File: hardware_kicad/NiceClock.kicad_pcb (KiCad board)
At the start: 2 copper layers, 198.2 x 198.2 mm, 294 parts, among them P1 CONN_01X04, U1 WS2811, U10 WS2811, U11 WS2811, U12 WS2811, U13 WS2811, U14 WS2811, U15 WS2811, U16 WS2811, U17 WS2811, U18 WS2811, U19 WS2811, U2 WS2811, U20 WS2811, U21 WS2811, U22 WS2811, U23 WS2811, U24 WS2811, U25 WS2811, U26 WS2811, U27 WS2811, U28 WS2811, U29 WS2811, U3 WS2811, U30 WS2811, U31 WS2811, U32 WS2811, U33 WS2811, U34 WS2811, U35 WS2811, U36 WS2811, U37 WS2811, U38 WS2811, U39 WS2811, U4 WS2811, U40 WS2811, U5 WS2811, U6 WS2811, U7 WS2811, U8 WS2811, U9 WS2811, Y1 8MHz

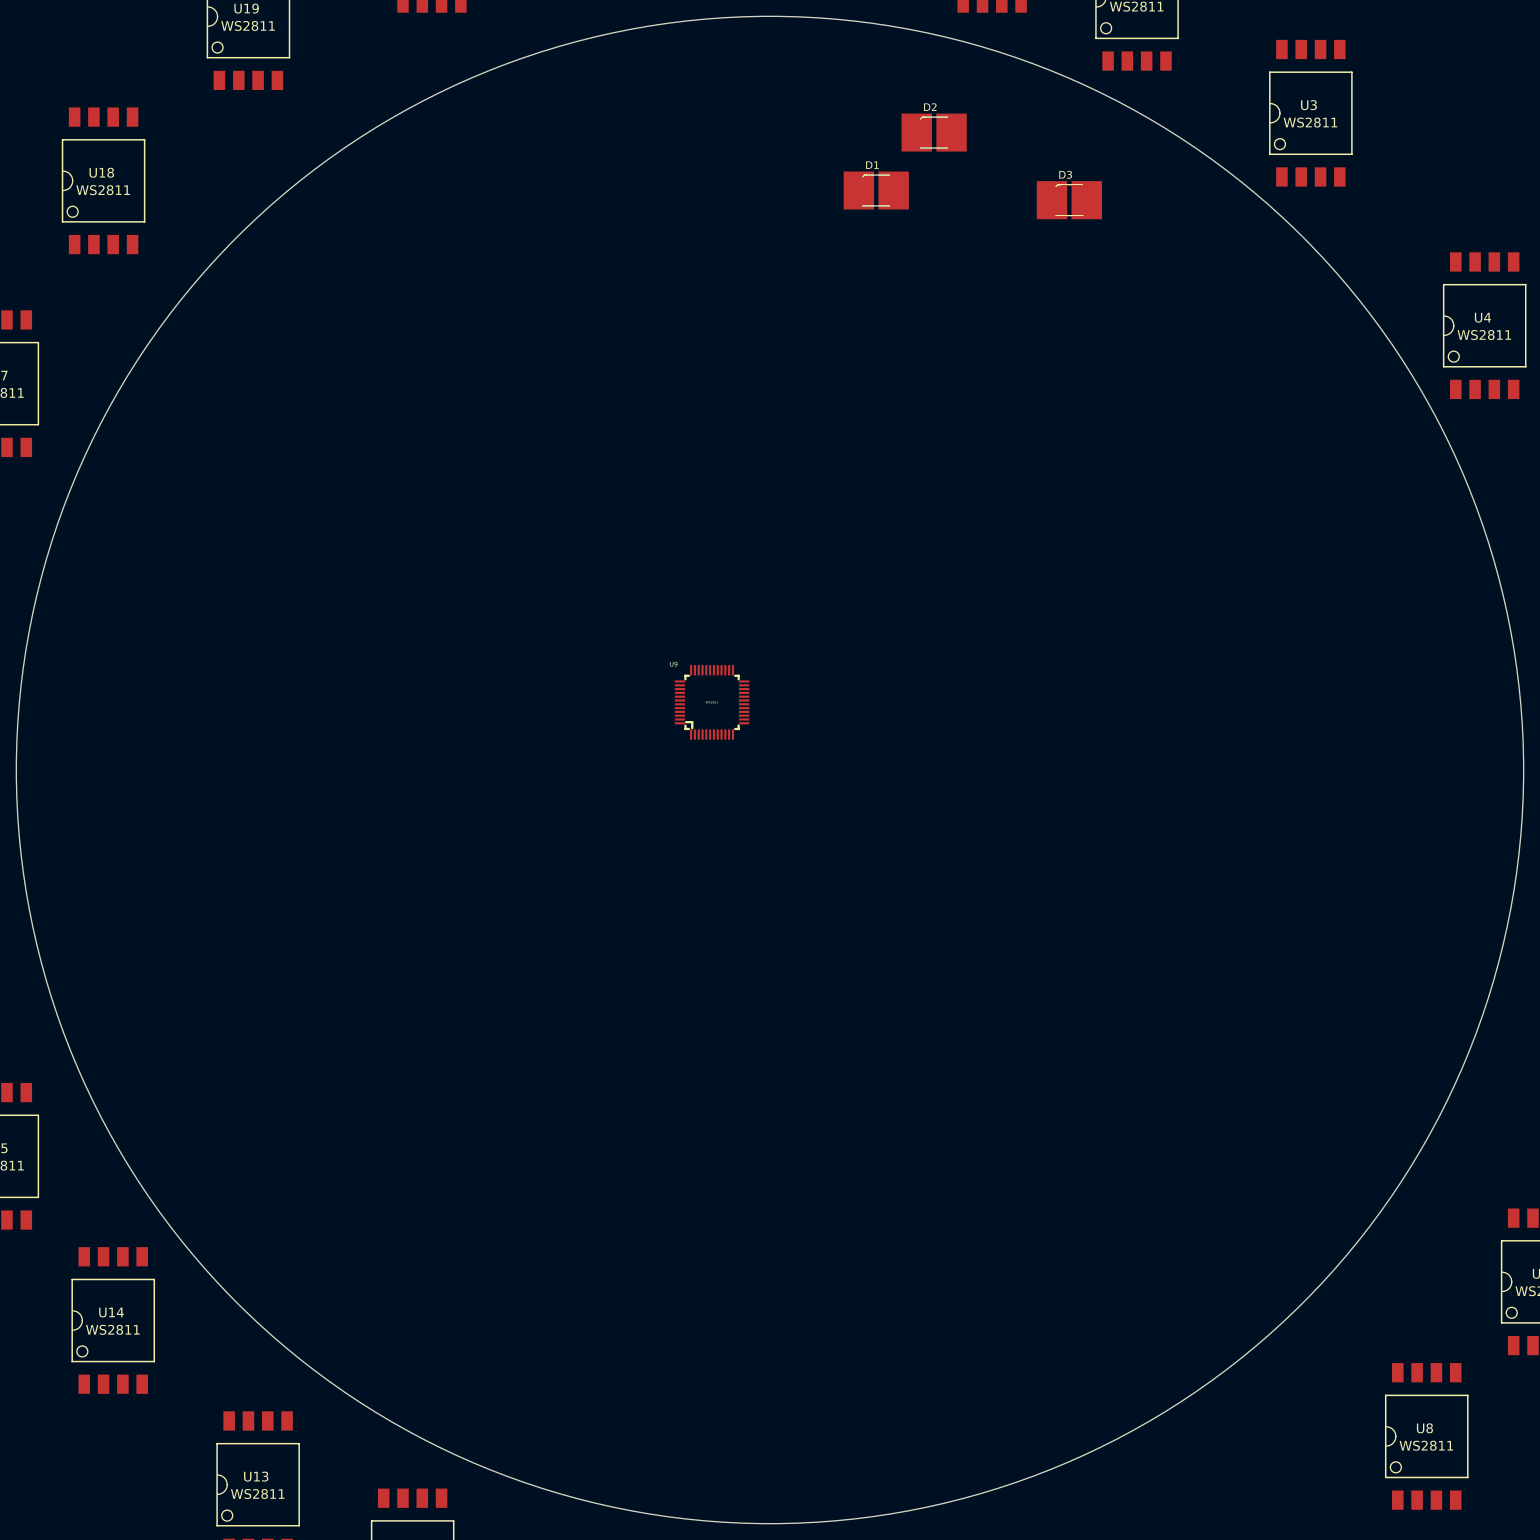
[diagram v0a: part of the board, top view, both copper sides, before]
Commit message: kicad changes + new eagle schematic
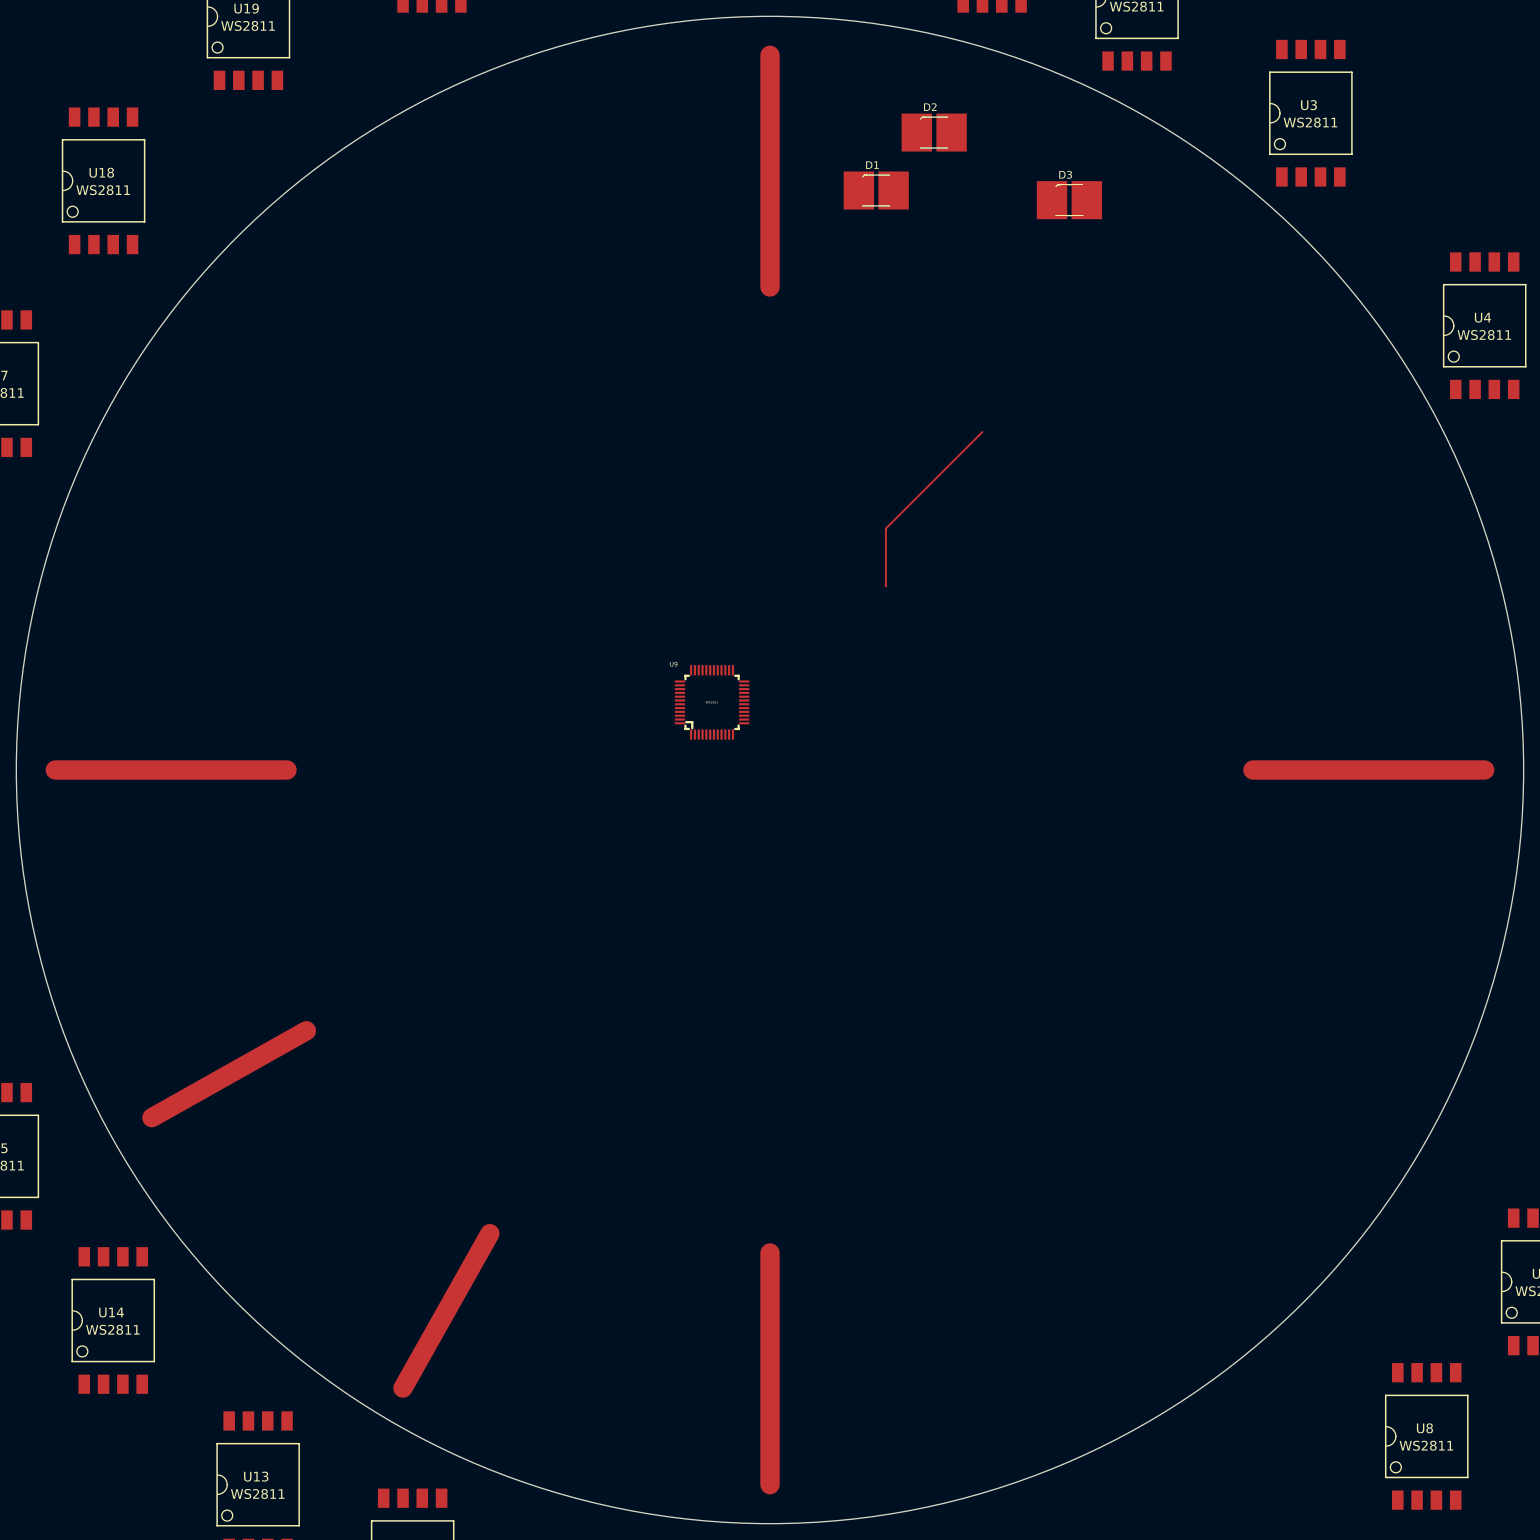
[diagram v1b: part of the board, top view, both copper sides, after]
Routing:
- net (no net): track 0.00 -> 194.1 mm
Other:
- net class Default: trace_width 0.25 -> 2.54
- net class c1 added: clearance 0.2, trace_width 0.5, via_dia 0.6, via_drill 0.4
- net class l1 added: clearance 0.2, trace_width 2.54, via_dia 0.6, via_drill 0.4
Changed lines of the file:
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@@
     (links 762)
     (no_connects 336)
-    (area 106.564302 45.604302 304.915698 243.955698)
+    (area -53.368333 -50.567001 382.370001 294.32819)
     (thickness 1.6)
-    (drawings 6)
-    (tracks 7)
+    (drawings 8)
+    (tracks 15)
     (zones 0)
     (modules 294)
@@
   )
   (setup
-    (last_trace_width 0.25)
+    (last_trace_width 2.54)
     (trace_clearance 0.2)
     (zone_clearance 0.508)
@@
   (net_class Default "This is the default net class."
     (clearance 0.2)
-    (trace_width 0.25)
+    (trace_width 2.54)
     (via_dia 0.6)
     (via_drill 0.4)
@@
     (add_net "Net-(U9-Pad7)")
   )
+  (net_class c1 ""
+    (clearance 0.2)
+    (trace_width 0.5)
+    (via_dia 0.6)
+    (via_drill 0.4)
+    (uvia_dia 0.3)
+    (uvia_drill 0.1)
+  )
+  (net_class l1 ""
+    (clearance 0.2)
+    (trace_width 2.54)
+    (via_dia 0.6)
+    (via_drill 0.4)
+    (uvia_dia 0.3)
+    (uvia_drill 0.1)
+  )
   (module Capacitors_SMD:C_0603_HandSoldering (layer F.Cu)
     (at 242.57 35.56 90)
@@
       (net 6 /OSC_OUT))
   )
+  (gr_circle (center 106.68 143.51) (end 179.07 210.82) (layer Dwgs.User) (width 0.2))
+  (gr_circle (center 205.74 243.84) (end 128.27 181.61) (layer Dwgs.User) (width 0.2))
   (target plus (at 205.74 144.78) (size 5) (width 0.15) (layer Edge.Cuts))
   (gr_line (start 382.27 88.9) (end 382.27 186.69) (angle 90) (layer Dwgs.User) (width 0.2))
@@
   (gr_line (start 205.74 38.1) (end 205.74 251.46) (angle 90) (layer Dwgs.User) (width 0.2))
   (gr_circle (center 205.74 144.78) (end 120.65 93.98) (layer Edge.Cuts) (width 0.15))
+  (segment (start 157.48 226.06) (end 168.91 205.74) (width 2.54) (layer F.Cu) (net 0))
+  (segment (start 124.46 190.5) (end 144.78 179.07) (width 2.54) (layer F.Cu) (net 0))
+  (segment (start 205.74 238.76) (end 205.74 208.28) (width 2.54) (layer F.Cu) (net 0))
+  (segment (start 111.76 144.78) (end 142.24 144.78) (width 2.54) (layer F.Cu) (net 0))
+  (segment (start 299.72 144.78) (end 269.24 144.78) (width 2.54) (layer F.Cu) (net 0))
+  (segment (start 205.74 50.8) (end 205.74 81.28) (width 2.54) (layer F.Cu) (net 0))
+  (segment (start 220.98 120.65) (end 220.98 113.03) (width 0.25) (layer F.Cu) (net 0))
+  (segment (start 220.98 113.03) (end 233.68 100.33) (width 0.25) (layer F.Cu) (net 0))
   (segment (start 255.26746 34.80054) (end 255.26746 28.10746) (width 0.25) (layer F.Cu) (net 264))
   (segment (start 255.26746 28.10746) (end 255.1 27.94) (width 0.25) (layer F.Cu) (net 264))
   (segment (start 240.03 31.75) (end 238.76 27.18308) (width 0.25) (layer F.Cu) (net 265))
-  (segment (start 238.76 27.18308) (end 238.75746 27.18054) (width 0.25) (layer F.Cu) (net 265) (status C00000))
+  (segment (start 238.76 27.18308) (end 238.75746 27.18054) (width 0.25) (layer F.Cu) (net 265))
   (segment (start 240.02746 31.75) (end 240.03 31.75) (width 0.25) (layer F.Cu) (net 265))
   (segment (start 240.03 31.75) (end 253.41054 31.75) (width 0.25) (layer F.Cu) (net 265))
-  (segment (start 253.41054 31.75) (end 252.9 27.94) (width 0.25) (layer F.Cu) (net 265) (status 800000))
+  (segment (start 253.41054 31.75) (end 252.9 27.94) (width 0.25) (layer F.Cu) (net 265))
 )

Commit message: kicad updates
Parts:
- moved U15 25.0 mm to (91.4, 174.0)
- moved U35 24.1 mm to (67.3, 174.0)
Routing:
- net GND: track 0.00 -> 32.3 mm
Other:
- net class Default: trace_width 2.54 -> 0.5
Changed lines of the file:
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@@
   (general
     (links 762)
-    (no_connects 336)
-    (area -53.368333 -50.567001 382.370001 294.32819)
+    (no_connects 335)
+    (area -53.368333 -50.567001 382.370001 343.308878)
     (thickness 1.6)
     (drawings 8)
-    (tracks 15)
+    (tracks 20)
     (zones 0)
     (modules 294)
@@
   )
   (setup
-    (last_trace_width 2.54)
+    (last_trace_width 0.5)
     (trace_clearance 0.2)
     (zone_clearance 0.508)
@@
   (net_class Default "This is the default net class."
     (clearance 0.2)
-    (trace_width 2.54)
+    (trace_width 0.5)
     (via_dia 0.6)
     (via_drill 0.4)
@@
   )
   (module custom_janh:SOP8 (layer F.Cu)
-    (at 104.14 195.58)
+    (at 91.44 173.99)
     (fp_text reference U15 (at -0.254 -1.016) (layer F.SilkS)
       (effects (font (thickness 0.3048)))
@@
   )
   (module custom_janh:SOP8 (layer F.Cu)
-    (at 74.93 196.85)
+    (at 67.31 173.99)
     (fp_text reference U35 (at -0.254 -1.016) (layer F.SilkS)
       (effects (font (thickness 0.3048)))
@@
   (segment (start 220.98 120.65) (end 220.98 113.03) (width 0.25) (layer F.Cu) (net 0))
   (segment (start 220.98 113.03) (end 233.68 100.33) (width 0.25) (layer F.Cu) (net 0))
+  (segment (start 71.11746 182.36946) (end 78.22946 182.36946) (width 0.5) (layer F.Cu) (net 1) (status 400000))
+  (segment (start 95.24746 186.69254) (end 95.24746 182.36946) (width 0.5) (layer F.Cu) (net 1) (status 800000))
+  (segment (start 92.71 189.23) (end 95.24746 186.69254) (width 0.5) (layer F.Cu) (net 1))
+  (segment (start 85.09 189.23) (end 92.71 189.23) (width 0.5) (layer F.Cu) (net 1))
+  (segment (start 78.22946 182.36946) (end 85.09 189.23) (width 0.5) (layer F.Cu) (net 1))
   (segment (start 255.26746 34.80054) (end 255.26746 28.10746) (width 0.25) (layer F.Cu) (net 264))
   (segment (start 255.26746 28.10746) (end 255.1 27.94) (width 0.25) (layer F.Cu) (net 264))

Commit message: reworked schematic + new board
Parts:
- removed C17, C18, C19, C20, C21, C22, C23, C24, C25, C26, C27, C28, C29, C30, C32, C33, C34, C35, C36, C37, C38, C39, C40, C41, C42, C43, C44, C47, C49: 100n, Capacitors_SMD:C_0603_HandSoldering
- removed C31: 100n, Capacitors_Tantalum_SMD:TantalC_SizeC_EIA-6032_Wave
- removed C45, C46: 20p, Capacitors_SMD:C_0603_HandSoldering
- removed C48: 10u, Capacitors_SMD:C_0603_HandSoldering
- removed R21, R22, R23, R24, R25, R26, R27, R28, R29, R30, R31, R32, R49, R50, R51, R52, R53, R54, R55, R56, R57, R58, R59, R60, R61, R62, R63, R64, R73, R74, R75, R76, R77, R78, R79, R80: 100R, Resistors_SMD:R_0603_HandSoldering
- removed R33, R34, R35, R36, R37, R38, R39, R40, R41, R42, R43, R44, R45, R46, R47, R48, R66, R67, R68, R69, R70, R71, R72: 33R, Resistors_SMD:R_0603_HandSoldering
- removed R65: 100k, Resistors_SMD:R_0603_HandSoldering
- removed R81, R82: 240R, Resistors_SMD:R_0603_HandSoldering
- removed R83: 400R, Resistors_SMD:R_0603_HandSoldering
- removed U10, U11, U12, U13, U14, U15, U16, U17, U18, U19, U20, U22, U23, U24, U25, U26, U27, U28, U29, U30, U31, U32, U33, U34, U35, U36, U37, U38, U39, U40: WS2811, custom_janh:SOP8
- removed U21: WS2811, TO_SOT_Packages_SMD:SOT-223
- added JP1: Jumper_NO_Small, custom_janh:Pin_Header_SMD_Angled_1x02, F.Cu at (375.9, 124.5)
- added JP2: Jumper_NO_Small, custom_janh:Pin_Header_SMD_Angled_1x02, F.Cu at (358.1, 124.5)
- C12, C13: value 100n -> 22p
- C15: value 100n -> 10u; footprint Capacitors_SMD:C_0603_HandSoldering -> Capacitors_Tantalum_SMD:TantalC_SizeC_EIA-6032_Wave
- P1: footprint Socket_Strips:Socket_Strip_Angled_1x04 -> custom_janh:Pin_Header_SMD_Angled_1x04
- R1, R10, R2, R3, R4, R8, R9: value 33R -> 1k
- R11, R12, R13, R5, R6, R7: value 33R -> 50R
- R14, R15: value 33R -> 200R
- R16: value 33R -> 100k
- R17, R20: value 100R -> 240R
- R18: value 100R -> 100k
- R19: value 100R -> 400R
- U1, U2, U3, U4, U5, U6, U7: value WS2811 -> WS2803; footprint custom_janh:SOP8 -> Housings_SOIC:SOIC-28_7.5x17.9mm_Pitch1.27mm
- U8: value WS2811 -> STM32F101C8; footprint custom_janh:SOP8 -> Housings_QFP:LQFP-48_7x7mm_Pitch0.5mm
- U9: value WS2811 -> LM317EMP; footprint SOP8:LQFP48 -> TO_SOT_Packages_SMD:SOT-223
- moved C13 435.1 mm to (396.1, 180.1)
- moved R12 433.7 mm to (391.8, 186.0)
- moved R5 431.2 mm to (391.8, 180.1)
- moved C5 428.8 mm to (387.4, 180.1)
- moved D104 427.8 mm to (391.4, 172.8)
- moved R6 427.0 mm to (383.0, 188.8)
- moved R10 426.8 mm to (375.2, 203.4)
- moved R11 423.1 mm to (366.1, 212.1)
- moved R19 423.0 mm to (378.5, 188.8)
- moved D105 421.9 mm to (392.2, 155.4)
- moved D103 421.8 mm to (380.8, 181.5)
- moved P1 420.6 mm to (339.1, 120.7)
- moved R7 420.3 mm to (366.3, 206.2)
- moved D109 418.7 mm to (368.4, 198.9)
- moved R14 418.6 mm to (357.4, 218.0)
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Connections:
- C1 pad 1: GND -> +3V3
- C1 pad 2: Net-(C1-Pad2) -> GND
- C10 pad 1: Net-(C10-Pad1) -> +3V3
- C10 pad 2: Net-(C10-Pad2) -> GND
- C11 pad 1: GND -> +3V3
- C11 pad 2: Net-(C11-Pad2) -> GND
- C12 pad 1: GND -> /OSC_IN
- C12 pad 2: Net-(C12-Pad2) -> GND
- C13 pad 1: GND -> /OSC_OUT
- C13 pad 2: Net-(C13-Pad2) -> GND
- C14 pad 1: Net-(C14-Pad1) -> +5V
- C14 pad 2: Net-(C14-Pad2) -> GND
- C15 pad 1: Net-(C15-Pad1) -> +3V3
- C15 pad 2: Net-(C15-Pad2) -> GND
- C16 pad 1: Net-(C16-Pad1) -> /NRST
- C16 pad 2: Net-(C16-Pad2) -> GND
- C2 pad 1: GND -> +3V3
- C2 pad 2: Net-(C2-Pad2) -> GND
- C3 pad 1: GND -> +3V3
- C3 pad 2: Net-(C3-Pad2) -> GND
- C4 pad 1: GND -> +3V3
- C4 pad 2: Net-(C4-Pad2) -> GND
- C5 pad 1: GND -> +3V3
- C5 pad 2: Net-(C5-Pad2) -> GND
- C6 pad 1: GND -> +3V3
- C6 pad 2: Net-(C6-Pad2) -> GND
- C7 pad 1: GND -> +3V3
- C7 pad 2: Net-(C7-Pad2) -> GND
- C8 pad 1: GND -> +3V3
- C8 pad 2: Net-(C8-Pad2) -> GND
- C9 pad 1: Net-(C9-Pad1) -> +3V3
- C9 pad 2: Net-(C9-Pad2) -> GND
- R1 pad 1: Net-(R1-Pad1) -> GND
- R10 pad 1: Net-(R10-Pad1) -> GND
- R14 pad 1: Net-(R14-Pad1) -> GND
- R15 pad 1: Net-(R15-Pad1) -> GND
- R16 pad 1: Net-(R16-Pad1) -> /BOOT0
- R16 pad 2: Net-(R16-Pad2) -> GND
- R17 pad 1: Net-(C1-Pad2) -> Net-(R17-Pad1)
- R17 pad 2: +5V -> +3V3
- R18 pad 1: Net-(C2-Pad2) -> /BOOT1
- R18 pad 2: +5V -> GND
- R19 pad 1: Net-(C3-Pad2) -> Net-(R17-Pad1)
- R19 pad 2: +5V -> GND
- R2 pad 1: Net-(R2-Pad1) -> GND
- R20 pad 1: Net-(C4-Pad2) -> +3V3
- R20 pad 2: +5V -> /NRST
- R3 pad 1: Net-(R3-Pad1) -> GND
- R4 pad 1: Net-(R4-Pad1) -> GND
- R8 pad 1: Net-(R8-Pad1) -> GND
- R9 pad 1: Net-(R9-Pad1) -> GND
- U1 pad 1: Net-(D1-Pad1) -> GND
- U1 pad 2: Net-(D2-Pad1) -> Net-(U1-Pad2)
- U1 pad 3: Net-(D3-Pad1) -> Net-(R1-Pad2)
- U1 pad 4: GND -> /LED_CLOCK
- U1 pad 5: Net-(R1-Pad2) -> /LED_DATA
- U1 pad 6: /LED_DATA -> Net-(D1-Pad1)
- U1 pad 7: Net-(U1-Pad7) -> Net-(D2-Pad1)
- U1 pad 8: Net-(C1-Pad2) -> Net-(D3-Pad1)
- U2 pad 1: Net-(D4-Pad1) -> GND
- U2 pad 2: Net-(D5-Pad1) -> Net-(U2-Pad2)
- U2 pad 3: Net-(D6-Pad1) -> Net-(R2-Pad2)
- U2 pad 4: GND -> Net-(U1-Pad25)
- U2 pad 5: Net-(R2-Pad2) -> Net-(R5-Pad1)
- U2 pad 6: Net-(R1-Pad1) -> Net-(D19-Pad1)
- U2 pad 7: Net-(U2-Pad7) -> Net-(D20-Pad1)
- U2 pad 8: Net-(C2-Pad2) -> Net-(D21-Pad1)
- U3 pad 1: Net-(D7-Pad1) -> GND
- U3 pad 2: Net-(D8-Pad1) -> Net-(U3-Pad2)
- U3 pad 3: Net-(D9-Pad1) -> Net-(R3-Pad2)
- U3 pad 4: GND -> Net-(U2-Pad25)
- U3 pad 5: Net-(R3-Pad2) -> Net-(R6-Pad1)
- U3 pad 6: Net-(R2-Pad1) -> Net-(D37-Pad1)
- U3 pad 7: Net-(U3-Pad7) -> Net-(D38-Pad1)
- U3 pad 8: Net-(C3-Pad2) -> Net-(D39-Pad1)
- U4 pad 1: Net-(D10-Pad1) -> GND
- U4 pad 2: Net-(D11-Pad1) -> Net-(U4-Pad2)
- U4 pad 3: Net-(D12-Pad1) -> Net-(R4-Pad2)
- U4 pad 4: GND -> Net-(U3-Pad25)
- U4 pad 5: Net-(R4-Pad2) -> Net-(R7-Pad1)
- U4 pad 6: Net-(R3-Pad1) -> Net-(D55-Pad1)
- U4 pad 7: Net-(U4-Pad7) -> Net-(D56-Pad1)
- U4 pad 8: Net-(C4-Pad2) -> Net-(D57-Pad1)
- U5 pad 1: Net-(D13-Pad1) -> GND
- U5 pad 2: Net-(D14-Pad1) -> Net-(U5-Pad2)
- U5 pad 3: Net-(D15-Pad1) -> Net-(R8-Pad2)
- U5 pad 4: GND -> Net-(U4-Pad25)
- U5 pad 5: Net-(R5-Pad2) -> Net-(R13-Pad1)
- U5 pad 6: Net-(R4-Pad1) -> Net-(D73-Pad1)
- U5 pad 7: Net-(U5-Pad7) -> Net-(D74-Pad1)
- U5 pad 8: Net-(C5-Pad2) -> Net-(D75-Pad1)
- U6 pad 1: Net-(D16-Pad1) -> GND
- U6 pad 2: Net-(D17-Pad1) -> Net-(U6-Pad2)
- U6 pad 3: Net-(D18-Pad1) -> Net-(R9-Pad2)
- U6 pad 4: GND -> Net-(U5-Pad25)
- U6 pad 5: Net-(R6-Pad2) -> Net-(R11-Pad1)
- U6 pad 6: Net-(R5-Pad1) -> Net-(D91-Pad1)
- U6 pad 7: Net-(U6-Pad7) -> Net-(D92-Pad1)
- U6 pad 8: Net-(C6-Pad2) -> Net-(D93-Pad1)
- U7 pad 1: Net-(D19-Pad1) -> GND
- U7 pad 2: Net-(D20-Pad1) -> Net-(U7-Pad2)
- U7 pad 3: Net-(D21-Pad1) -> Net-(R10-Pad2)
- U7 pad 4: GND -> Net-(U6-Pad25)
- U7 pad 5: Net-(R7-Pad2) -> Net-(R12-Pad1)
- U7 pad 6: Net-(R6-Pad1) -> Net-(D109-Pad1)
- U7 pad 7: Net-(U7-Pad7) -> Net-(D110-Pad1)
- U7 pad 8: Net-(C7-Pad2) -> Net-(D111-Pad1)
- U8 pad 1: Net-(D22-Pad1) -> +3V3
- U8 pad 2: Net-(D23-Pad1) -> Net-(U8-Pad2)
- U8 pad 3: Net-(D24-Pad1) -> Net-(U8-Pad3)
- U8 pad 4: GND -> Net-(U8-Pad4)
- U8 pad 5: Net-(R8-Pad2) -> /OSC_IN
- U8 pad 6: Net-(R7-Pad1) -> /OSC_OUT
- U8 pad 7: Net-(U8-Pad7) -> /NRST
- U8 pad 8: Net-(C8-Pad2) -> GND
- U9 pad 1: Net-(D25-Pad1) -> Net-(R17-Pad1)
- U9 pad 2: Net-(D26-Pad1) -> +3V3
- U9 pad 3: Net-(D27-Pad1) -> +5V
- U9 pad 4: GND -> (no net)
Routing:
- net (no net): track 194.1 -> 0.00 mm
- net GND: track 32.3 -> 0.00 mm
- net Net-(R1-Pad2): track 22.0 -> 0.00 mm
- net Net-(R1-Pad1): track 6.93 -> 0.00 mm
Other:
- board size 198.2 x 198.2 mm -> 249 x 249 mm
- net class c1 removed
- net class l1 removed
- net class power added: clearance 0.2, trace_width 0.5, via_dia 0.6, via_drill 0.4

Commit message: placed LEDs and other stuff
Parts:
- removed R20: 240R, Resistors_SMD:R_0603_HandSoldering
- moved D103 332.6 mm to (64.0, 80.3), turned to 54 degrees
- moved D105 331.6 mm to (71.5, 71.0), turned to 48 degrees
- moved D104 326.2 mm to (76.1, 89.1), turned to 54 degrees
- moved D92 326.1 mm to (57.2, 147.3), turned to 90 degrees
- moved D93 323.8 mm to (42.8, 135.4), turned to 84 degrees
- moved D102 315.2 mm to (70.5, 97.8), turned to 60 degrees
- moved D109 314.1 mm to (89.2, 55.1), turned to 36 degrees
- moved D83 313.0 mm to (52.1, 193.7), turned to 114 degrees
- moved D85 306.2 mm to (47.8, 182.6), turned to 108 degrees
- moved D107 305.4 mm to (79.9, 62.6), turned to 42 degrees
- moved D82 303.9 mm to (70.5, 196.8), turned to 120 degrees
- moved D97 303.5 mm to (47.8, 112.1), turned to 72 degrees
- moved D89 301.3 mm to (42.8, 159.2), turned to 96 degrees
- moved D106 300.2 mm to (82.6, 81.1), turned to 48 degrees
- moved D98 299.9 mm to (62.0, 116.7), turned to 72 degrees
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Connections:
- net /NRST renamed Net-(C16-Pad1)
